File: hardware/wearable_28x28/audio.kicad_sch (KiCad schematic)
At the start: 15 parts, among them U30 TLV9001IDCKR

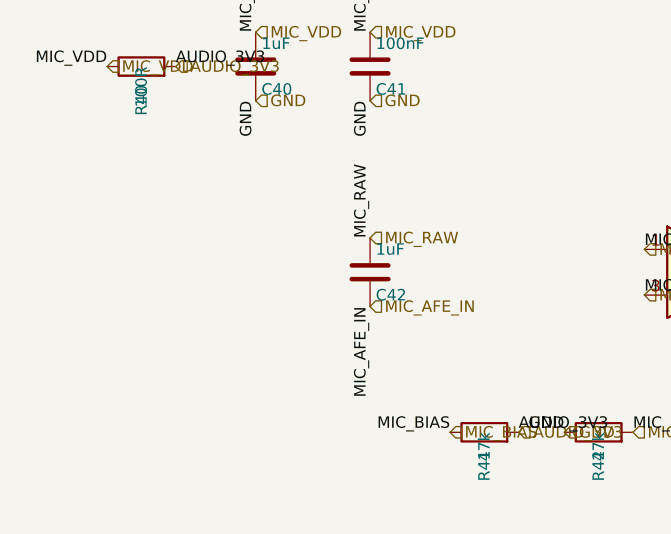
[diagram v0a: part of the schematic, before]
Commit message: Regenerate hierarchies with selected EVT parts
Co-authored-by: illiapliukhin <illiapliukhin@users.noreply.github.com>
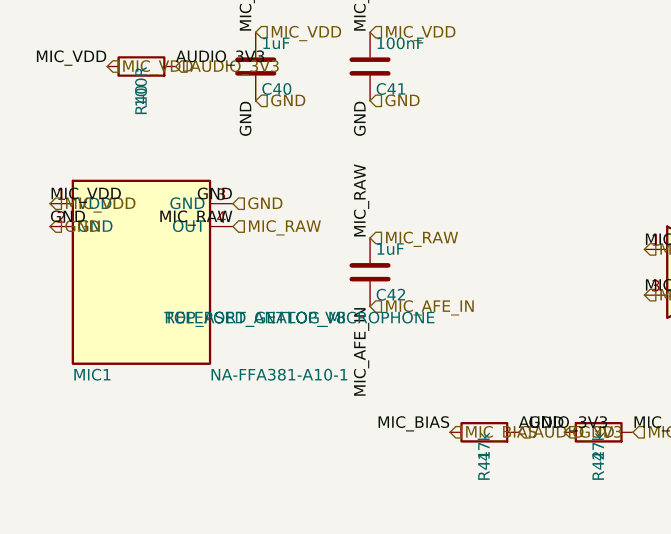
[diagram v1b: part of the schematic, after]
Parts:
- added MIC1: NA-FFA381-A10-1, PartSignal_Packages:Gettop_NA-FFA381-A10-1_TopPort_Microphone, symbol PartSignal_Platform:NA-FFA381-A10-1
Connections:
- net GND: now also MIC1.2 (GND), MIC1.3 (GND)
- net MIC_RAW: now also MIC1.4 (OUT)
- net MIC_VDD: now also MIC1.1 (VDD)
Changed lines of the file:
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@@
+		)
+	)
+	(label "MIC_VDD"
+		(at 20.32 53.34 0)
+		(effects
+			(font
+				(size 1.27 1.27)
+			)
+			(justify left bottom)
 		)
 	)
@@
 		)
 	)
+	(label "GND"
+		(at 20.32 55.88 0)
+		(effects
+			(font
+				(size 1.27 1.27)
+			)
+			(justify left bottom)
+		)
+	)
 	(label "MIC_VDD"
 		(at 55.88 34.29 90)
@@
 		)
 	)
+	(label "GND"
+		(at 40.64 53.34 180)
+		(effects
+			(font
+				(size 1.27 1.27)
+			)
+			(justify right bottom)
+		)
+	)
 	(label "MIC_VDD"
 		(at 43.18 34.29 90)
@@
 		)
 	)
+	(label "MIC_RAW"
+		(at 40.64 55.88 180)
+		(effects
+			(font
+				(size 1.27 1.27)
+			)
+			(justify right bottom)
+		)
+	)
 	(label "MIC_AFE_OUT"
 		(at 135.89 50.8 0)
@@
 		)
 	)
+	(hierarchical_label "GND"
+		(shape input)
+		(at 20.32 55.88 0)
+		(effects
+			(font
+				(size 1.27 1.27)
+			)
+			(justify left)
+		)
+	)
 	(hierarchical_label "MIC_AFE_OUT"
 		(shape input)
@@
 		)
 	)
+	(hierarchical_label "MIC_RAW"
+		(shape input)
+		(at 40.64 55.88 0)
+		(effects
+			(font
+				(size 1.27 1.27)
+			)
+			(justify left)
+		)
+	)
 	(hierarchical_label "AUDIO_3V3"
 		(shape input)
@@
 		)
 	)
+	(hierarchical_label "GND"
+		(shape input)
+		(at 40.64 53.34 0)
+		(effects
+			(font
+				(size 1.27 1.27)
+			)
+			(justify left)
+		)
+	)
 	(hierarchical_label "MIC_VDD"
 		(shape input)
@@
 		(shape input)
 		(at 93.98 82.55 0)
+		(effects
+			(font
+				(size 1.27 1.27)
+			)
+			(justify left)
+		)
+	)
+	(hierarchical_label "MIC_VDD"
+		(shape input)
+		(at 20.32 53.34 0)
 		(effects
 			(font
@@
 					(unit 1)
 				)
+			)
+		)
+	)
+	(symbol
+		(lib_id "PartSignal_Platform:NA-FFA381-A10-1")
+		(at 30.48 60.96 0)
+		(unit 1)
+		(body_style 1)
+		(exclude_from_sim no)
+		(in_bom yes)
+		(on_board yes)
+		(in_pos_files yes)
+		(dnp no)
+		(property "Reference" "MIC1"
+			(at 22.86 72.39 0)
+			(show_name no)
+			(do_not_autoplace no)
+			(effects
+				(font
+					(size 1.27 1.27)
+				)
+				(justify left)
+			)
+		)
+		(property "Value" "NA-FFA381-A10-1"
+			(at 38.1 72.39 0)
+			(show_name no)
+			(do_not_autoplace no)
+			(effects
+				(font
+					(size 1.27 1.27)
+				)
+				(justify left)
+			)
+		)
+		(property "Footprint" "PartSignal_Packages:Gettop_NA-FFA381-A10-1_TopPort_Microphone"
+			(at 30.48 60.96 0)
+			(hide yes)
+			(show_name no)
+			(do_not_autoplace no)
+			(effects
+				(font
+					(size 1.27 1.27)
+				)
+			)
+		)
+		(property "Datasheet" ""
+			(at 30.48 60.96 0)
+			(show_name no)
+			(do_not_autoplace no)
+			(effects
+				(font
+					(size 1.27 1.27)
+				)
+			)
+		)
+		(property "Description" ""
+			(at 30.48 60.96 0)
+			(show_name no)
+			(do_not_autoplace no)
+			(effects
+				(font
+					(size 1.27 1.27)
+				)
+			)
+		)
+		(property "Function" "TOP_PORT_ANALOG_MICROPHONE"
+			(at 33.02 66.0399 0)
+			(show_name no)
+			(do_not_autoplace no)
+			(effects
+				(font
+					(size 1.27 1.27)
+				)
+				(justify left)
+			)
+		)
+		(property "FootprintStatus" "RELEASED_GETTOP_V8"
+			(at 33.02 66.0399 0)
+			(show_name no)
+			(do_not_autoplace no)
+			(effects
+				(font
+					(size 1.27 1.27)
+				)
+				(justify left)
+			)
+		)
+		(pin "1"
+		)
+		(pin "2"
+		)
+		(pin "3"
+		)
+		(pin "4"
+		)
+		(instances
+			(project ""
+				(path "/ab3aff4e-d443-56a3-bff5-538953355925"
+					(reference "MIC1")
+					(unit 1)
+				)
